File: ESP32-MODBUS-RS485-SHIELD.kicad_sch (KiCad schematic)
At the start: 27 parts

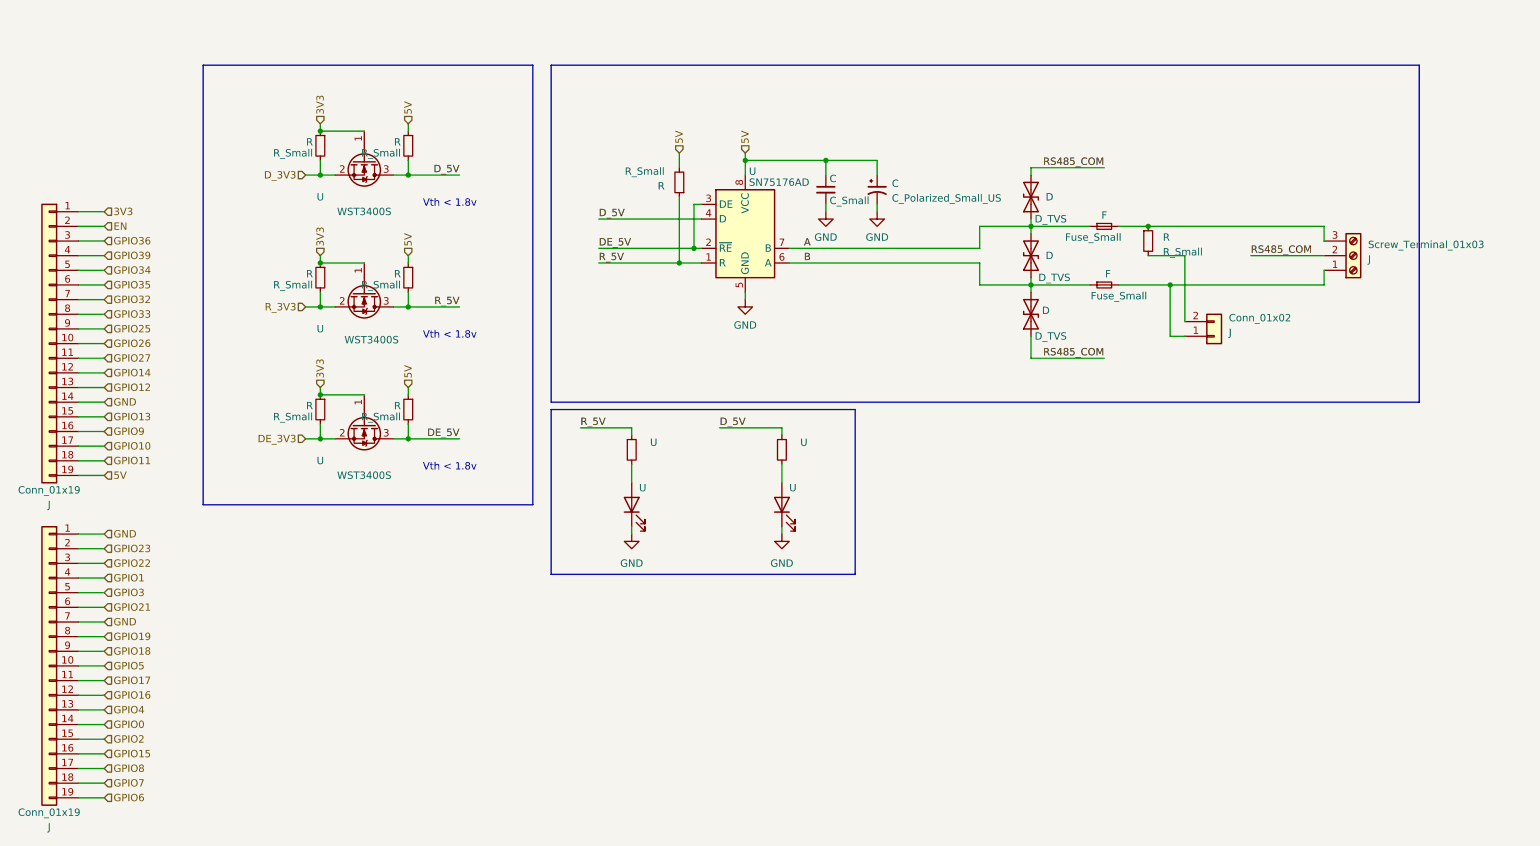
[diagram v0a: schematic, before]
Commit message: Update ESP32-MODBUS-RS485-SHIELD.kicad_sch
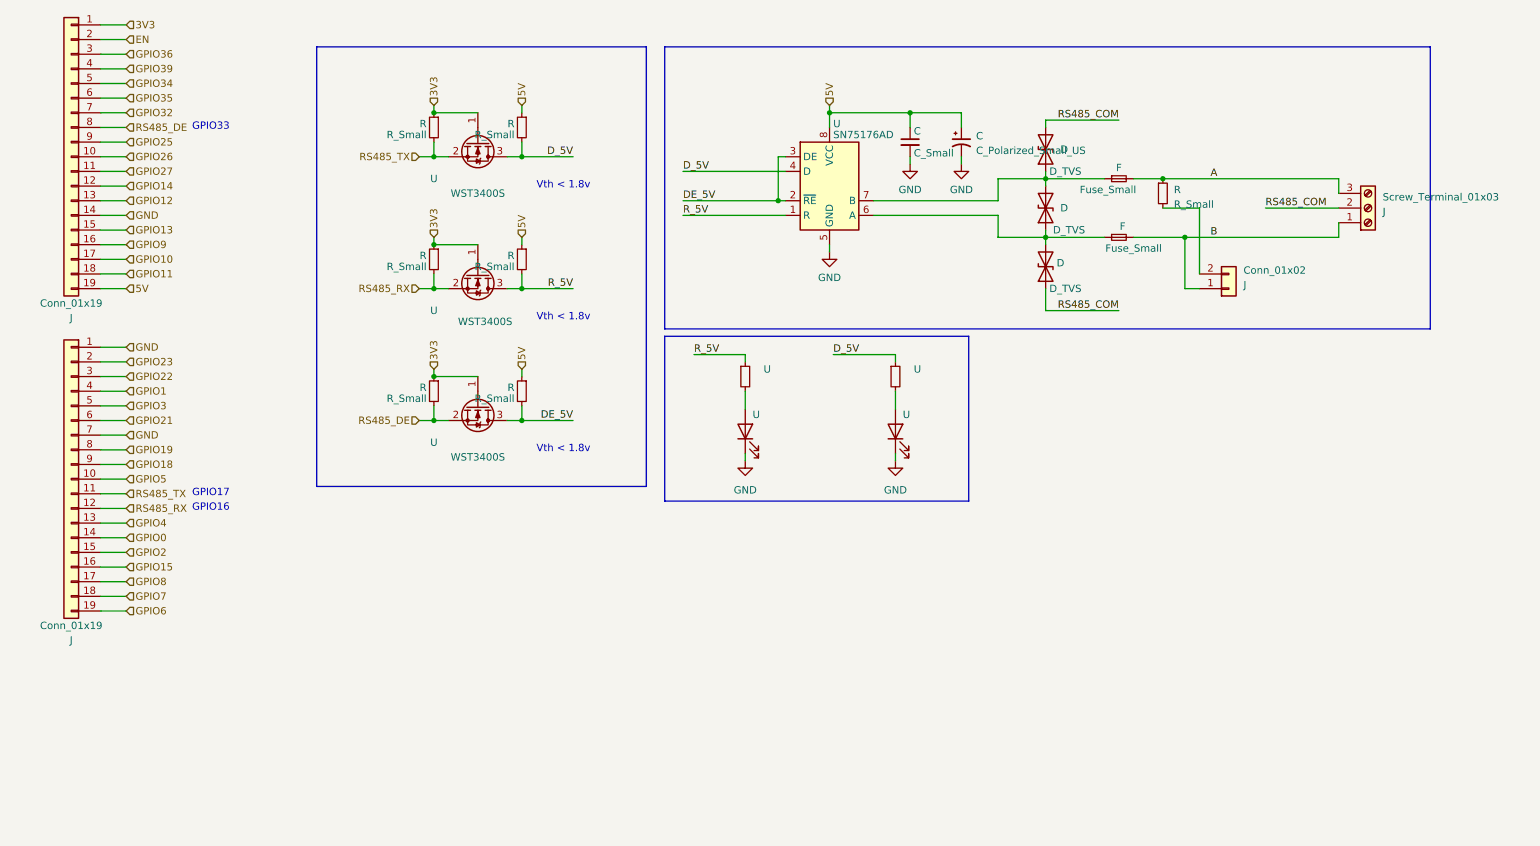
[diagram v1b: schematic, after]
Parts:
- removed R: R_Small, symbol Device:R_Small
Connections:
- net GPIO17 is gone; now on net RS485_TX: J.11 (Pin_11)
- net GPIO33 is gone; now on net RS485_DE: J.8 (Pin_8)
- net R_3V3 is gone; now on net RS485_RX: R.2, U.2 (S)
- net A: now also F.2, J.3 (Pin_3), R.1; no longer D.1 (A1), D.2 (A2), F.1, U.7 (B)
- net B: now also F.2, J.1 (Pin_1), J.1 (Pin_1); no longer D.1 (A1), D.2 (A2), F.1, U.6 (A)
- net DE_3V3 renamed RS485_DE
- net D_3V3 renamed RS485_TX
- net GPIO16 renamed RS485_RX
- new net: D.1 (A1), D.2 (A2), F.1, U.7 (B)
- new net: D.1 (A1), D.2 (A2), F.1, U.6 (A)
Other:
- note added: "GPIO16"
- note added: "GPIO17"
- note added: "GPIO33"
- moved on the sheet: C, D, F, J, R, U

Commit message: update
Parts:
- added F: Polyfuse_Small, symbol Device:Polyfuse_Small
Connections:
- net 5V: now also F.2; no longer J.19 (Pin_19)
- new net: F.1, J.19 (Pin_19)
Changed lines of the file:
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@@
+    (stroke (width 0) (type default))
+  )
+  (wire (pts (xy 44.45 66.675) (xy 45.72 66.675))
     (stroke (width 0) (type default))
   )
@@
   )
   (wire (pts (xy 27.94 64.135) (xy 32.385 64.135))
+    (stroke (width 0) (type default))
+  )
+  (wire (pts (xy 27.94 66.675) (xy 39.37 66.675))
     (stroke (width 0) (type default))
   )
@@
     (stroke (width 0) (type default))
   )
-  (wire (pts (xy 27.94 66.675) (xy 32.385 66.675))
-    (stroke (width 0) (type default))
-  )
   (wire (pts (xy 183.515 57.785) (xy 191.77 57.785))
     (stroke (width 0) (type default))
@@
     (effects (font (size 1.27 1.27)) (justify left))
   )
-  (hierarchical_label "5V" (shape input) (at 32.385 66.675 0) (fields_autoplaced)
+  (hierarchical_label "5V" (shape input) (at 45.72 66.675 0) (fields_autoplaced)
     (effects (font (size 1.27 1.27)) (justify left))
   )
@@
     )
     (property "Datasheet" "~" (id 3) (at 168.275 41.275 0)
+      (effects (font (size 1.27 1.27)) hide)
+    )
+    (pin "1")
+    (pin "2")
+  )
+  (symbol (lib_id "Device:Polyfuse_Small") (at 41.91 66.675 90) (unit 1)
+    (in_bom yes) (on_board yes)
+    (default_instance (reference "F") (unit 1) (value "Polyfuse_Small") (footprint ""))
+    (property "Reference" "F" (id 0) (at 42.545 64.135 90)
+      (effects (font (size 1.27 1.27)))
+    )
+    (property "Value" "Polyfuse_Small" (id 1) (at 41.91 68.58 90)
+      (effects (font (size 1.27 1.27)))
+    )
+    (property "Footprint" "" (id 2) (at 46.99 65.405 0)
+      (effects (font (size 1.27 1.27)) (justify left) hide)
+    )
+    (property "Datasheet" "~" (id 3) (at 41.91 66.675 0)
       (effects (font (size 1.27 1.27)) hide)
     )
@@
       (reference "F2") (unit 1) (value "MF-MSMF050-2") (footprint "Library:Fuse_1812_4532Metric")
     )
+    (path "/2256db5e-4433-4943-9437-d8cdfc5ec719"
+      (reference "F3") (unit 1) (value "Polyfuse_Small") (footprint "Fuse:Fuse_1206_3216Metric")
+    )
     (path "/44e5e4ec-1772-42d9-b369-eead3a6d2b2a"

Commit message: update
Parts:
- C3: renamed from C; value C_Small -> 100nF; footprint (none) -> Library:C_0603_1608Metric
- C5: renamed from C; value C_Polarized_Small_US -> 10uF; footprint (none) -> Library:CP_EIA-3528-21_Kemet-B
- D33, D34, D35: renamed from D; value D_TVS -> SMAJ6.5CA; footprint (none) -> Library:D_SMA
- D36: renamed from U; value (none) -> GREEN; footprint (none) -> Library:LED_0603_1608Metric
- D37: renamed from U; value (none) -> RED; footprint (none) -> Library:LED_0603_1608Metric
- F1, F2: renamed from F; value Fuse_Small -> MF-MSMF050-2; footprint (none) -> Library:Fuse_1812_4532Metric
- F3: renamed from F; footprint (none) -> Fuse:Fuse_1206_3216Metric
- J1, J2: renamed from J; footprint (none) -> Connector_PinSocket_2.54mm:PinSocket_1x19_P2.54mm_Vertical
- J10: renamed from J; footprint (none) -> Library:PinHeader_1x02_P2.54mm_Vertical
- J9: renamed from J; value Screw_Terminal_01x03 -> RS485; footprint (none) -> Connector_Phoenix_MC:PhoenixContact_MC_1,5_3-G-3.5_1x03_P3.50mm_Horizontal
- Q17, Q18, Q19: renamed from U; value (none) -> WST3400S; footprint (none) -> Library:SOT-23
- R36: renamed from R; value R_Small -> 120; footprint (none) -> Library:R_0603_1608Metric
- R38, R39, R40, R41, R42, R43: renamed from R; value R_Small -> 10k; footprint (none) -> Library:R_0603_1608Metric
- R45, R47: renamed from U; value (none) -> 470R; footprint (none) -> Library:R_0603_1608Metric
- U11: renamed from U; footprint Package_SO:SOIC-8_3.9x4.9mm_P1.27mm -> Library:SO08

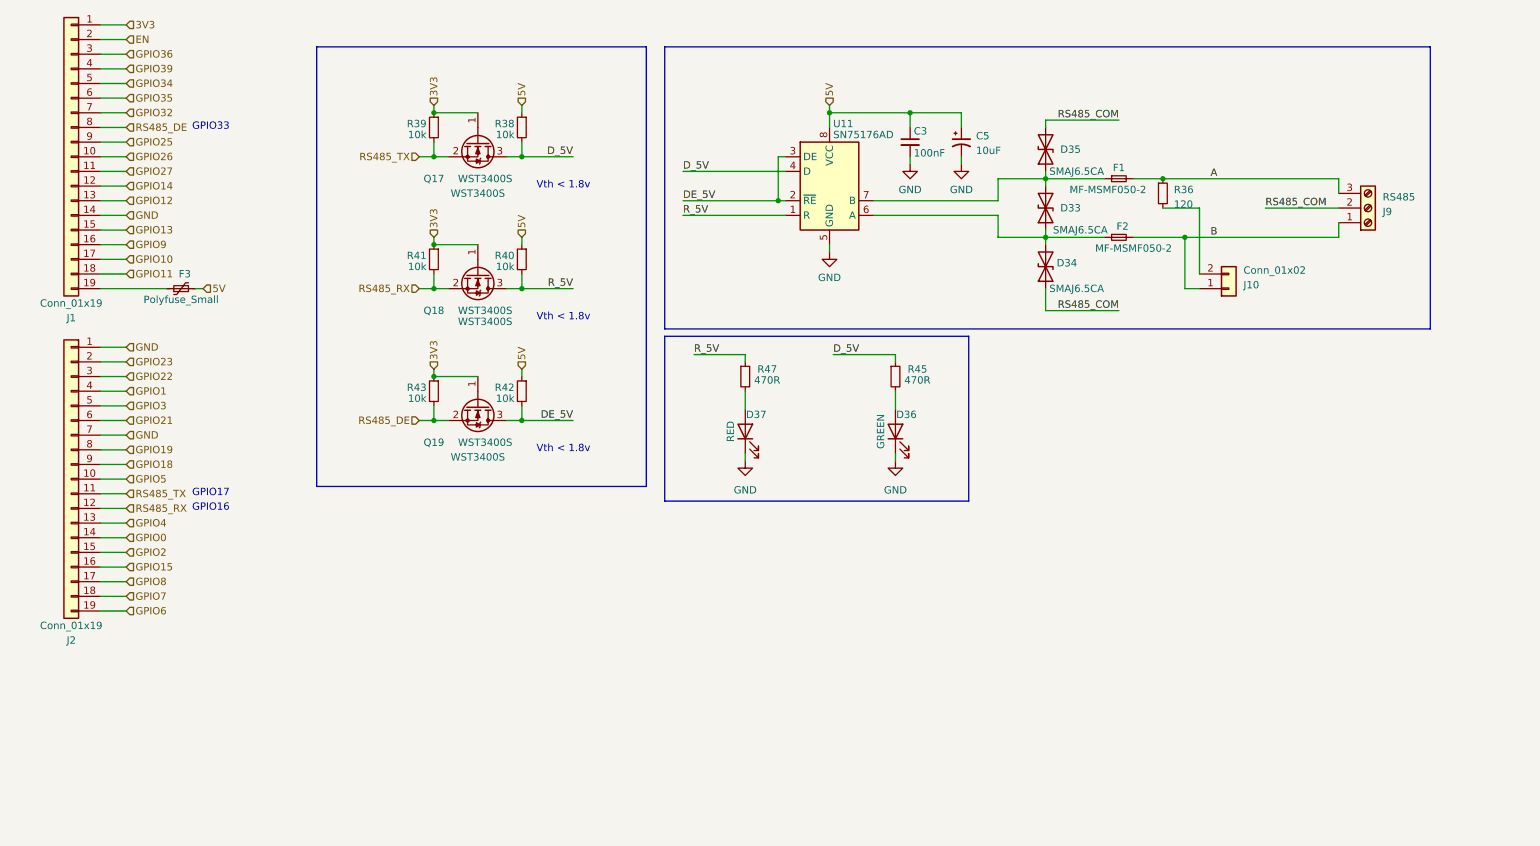
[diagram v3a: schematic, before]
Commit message: Update ESP32-MODBUS-RS485-SHIELD.kicad_sch
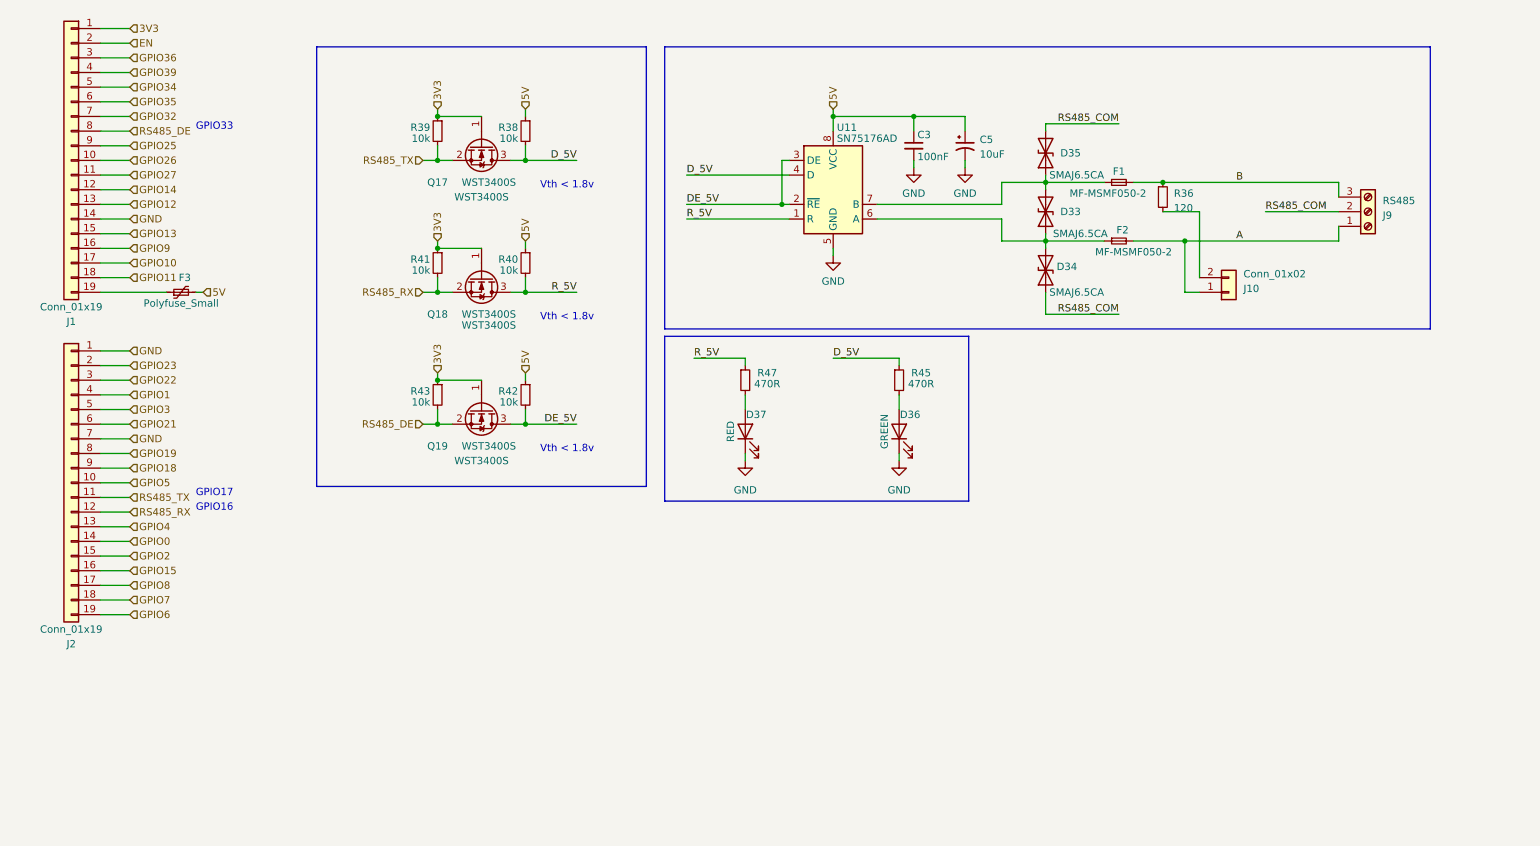
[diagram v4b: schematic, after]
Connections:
- net A: now also F2.2, J10.1 (Pin_1), J9.1 (Pin_1); no longer F1.2, J9.3 (Pin_3), R36.1
- net B: now also F1.2, J9.3 (Pin_3), R36.1; no longer F2.2, J10.1 (Pin_1), J9.1 (Pin_1)
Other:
- moved on the sheet: C3, C5, D33, D34, D35, D36, F1, F2, F3, J1, J10, J2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
